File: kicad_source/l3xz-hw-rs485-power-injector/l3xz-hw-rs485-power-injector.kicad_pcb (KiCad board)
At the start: 2 copper layers, 38 x 55 mm, 14 parts, among them J1 PowerPole, J2 Conn_01x02, J3 Conn_01x03, J4 SM04B-GHS-TB, J5 EH_S4B-EH, J6 EH_S4B-EH

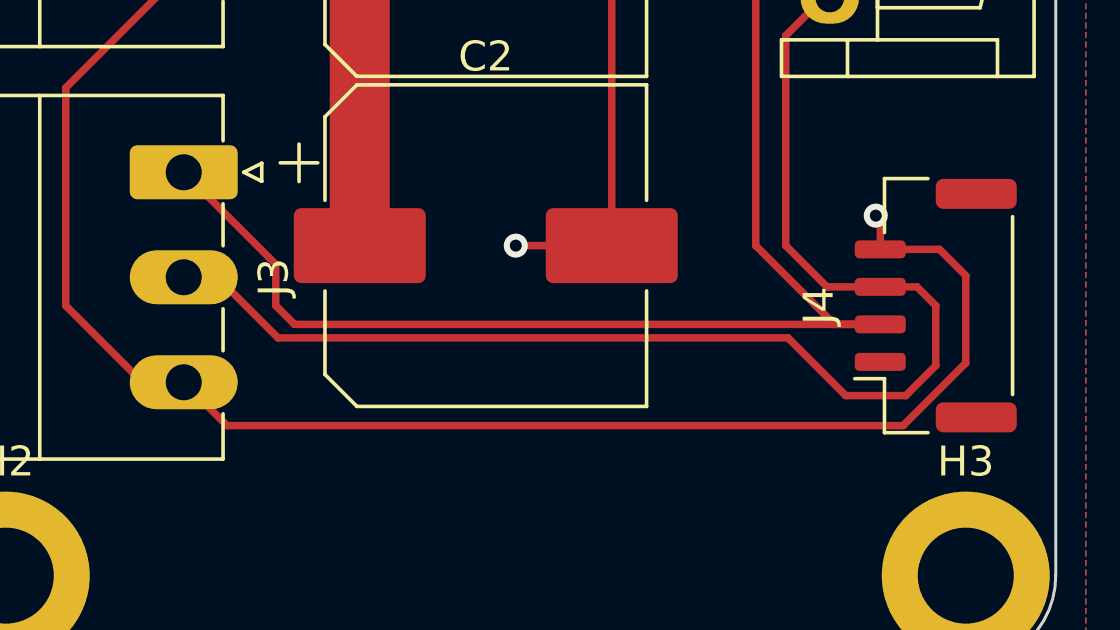
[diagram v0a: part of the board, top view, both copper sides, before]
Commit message: added resistor to connect JST GH connector to +BATT
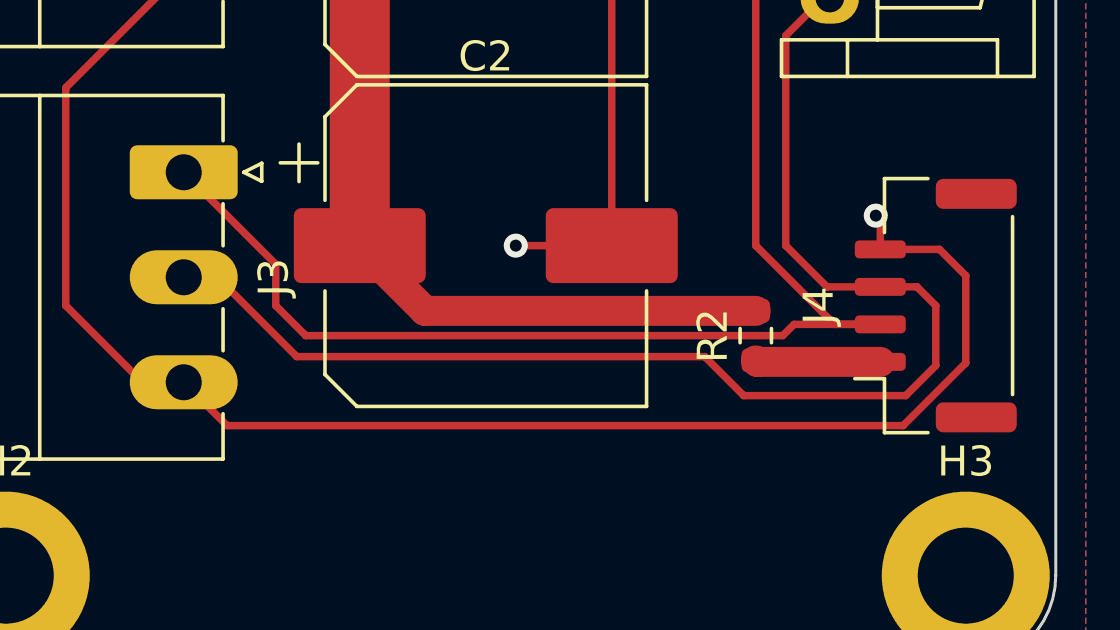
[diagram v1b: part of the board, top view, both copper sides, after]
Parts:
- added R2: DNI, Resistor_SMD:R_0603_1608Metric, F.Cu at (154.0, 97.0)
- C1, C2: value C_Polarized -> 220 uF / 50 V
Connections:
- J4 pad 1: unconnected-(J4-Pad1) -> /BATT_R
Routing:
- net +BATT: track 72.1 -> 86.2 mm
- net /BATT_R: track 0.00 -> 4.17 mm
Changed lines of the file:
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@@
   )
   (paper "A4")
+  (title_block
+    (title "l3xz-hw-rs485-power-injector")
+    (date "2023-01-21")
+    (rev "0.1")
+    (company "107-systems")
+  )
   (layers
     (0 "F.Cu" signal)
@@
   (net 3 "/RS485_A")
   (net 4 "/RS485_B")
-  (net 5 "unconnected-(J4-Pad1)")
+  (net 5 "/BATT_R")
   (net 6 "Net-(D1-Pad2)")
   (net 7 "unconnected-(H1-Pad1)")
@@
     (fp_line (start -4.125 2.45) (end 4.125 2.45) (layer "F.Fab") (width 0.1))
     (pad "1" smd roundrect (at -1.875 -1.85 90) (size 0.6 1.7) (layers "F.Cu" "F.Paste" "F.Mask") (roundrect_rratio 0.25)
-      (net 5 "unconnected-(J4-Pad1)") (pinfunction "Pin_1") (pintype "passive+no_connect"))
+      (net 5 "/BATT_R") (pinfunction "Pin_1") (pintype "passive"))
     (pad "2" smd roundrect (at -0.625 -1.85 90) (size 0.6 1.7) (layers "F.Cu" "F.Paste" "F.Mask") (roundrect_rratio 0.25)
       (net 3 "/RS485_A") (pinfunction "Pin_2") (pintype "passive"))
@@
       (effects (font (size 1 1) (thickness 0.15)))
     )
-    (fp_text value "C_Polarized" (at 0 6.3) (layer "F.Fab")
+    (fp_text value "220 uF / 50 V" (at 0 6.3) (layer "F.Fab")
       (effects (font (size 1 1) (thickness 0.15)))
     )
@@
     (model "${KICAD6_3DMODEL_DIR}/generationmake/PP 15-45 (Std)-02-08-STEP.stp"
       (offset (xyz -3.95 -13.1 16))
+      (scale (xyz 1 1 1))
+      (rotate (xyz 0 0 0))
+    )
+  )
+  (footprint "Resistor_SMD:R_0603_1608Metric" (layer "F.Cu")
+    (at 154 97 90)
+    (descr "Resistor SMD 0603 (1608 Metric), square (rectangular) end terminal, IPC_7351 nominal, (Body size source: IPC-SM-782 page 72, https://www.pcb-3d.com/wordpress/wp-content/uploads/ipc-sm-782a_amendment_1_and_2.pdf), generated with kicad-footprint-generator")
+    (tags "resistor")
+    (property "Sheetfile" "l3xz-hw-rs485-power-injector.kicad_sch")
+    (property "Sheetname" "")
+    (attr smd)
+    (fp_text reference "R2" (at 0 -1.43 90) (layer "F.SilkS")
+      (effects (font (size 1 1) (thickness 0.15)))
+    )
+    (fp_text value "DNI" (at 0 1.43 90) (layer "F.Fab")
+      (effects (font (size 1 1) (thickness 0.15)))
+    )
+    (fp_text user "${REFERENCE}" (at 0 0 90) (layer "F.Fab")
+      (effects (font (size 0.4 0.4) (thickness 0.06)))
+    )
+    (fp_line (start -0.237258 -0.5225) (end 0.237258 -0.5225) (layer "F.SilkS") (width 0.12))
+    (fp_line (start -0.237258 0.5225) (end 0.237258 0.5225) (layer "F.SilkS") (width 0.12))
+    (fp_line (start -1.48 0.73) (end -1.48 -0.73) (layer "F.CrtYd") (width 0.05))
+    (fp_line (start 1.48 -0.73) (end 1.48 0.73) (layer "F.CrtYd") (width 0.05))
+    (fp_line (start 1.48 0.73) (end -1.48 0.73) (layer "F.CrtYd") (width 0.05))
+    (fp_line (start -1.48 -0.73) (end 1.48 -0.73) (layer "F.CrtYd") (width 0.05))
+    (fp_line (start 0.8 0.4125) (end -0.8 0.4125) (layer "F.Fab") (width 0.1))
+    (fp_line (start -0.8 0.4125) (end -0.8 -0.4125) (layer "F.Fab") (width 0.1))
+    (fp_line (start 0.8 -0.4125) (end 0.8 0.4125) (layer "F.Fab") (width 0.1))
+    (fp_line (start -0.8 -0.4125) (end 0.8 -0.4125) (layer "F.Fab") (width 0.1))
+    (pad "1" smd roundrect (at -0.825 0 90) (size 0.8 0.95) (layers "F.Cu" "F.Paste" "F.Mask") (roundrect_rratio 0.25)
+      (net 5 "/BATT_R") (pintype "passive"))
+    (pad "2" smd roundrect (at 0.825 0 90) (size 0.8 0.95) (layers "F.Cu" "F.Paste" "F.Mask") (roundrect_rratio 0.25)
+      (net 1 "+BATT") (pintype "passive"))
+    (model "${KICAD6_3DMODEL_DIR}/Resistor_SMD.3dshapes/R_0603_1608Metric.wrl"
+      (offset (xyz 0 0 0))
       (scale (xyz 1 1 1))
       (rotate (xyz 0 0 0))
@@
       (effects (font (size 1 1) (thickness 0.15)))
     )
-    (fp_text value "C_Polarized" (at 0 6.3) (layer "F.Fab")
+    (fp_text value "220 uF / 50 V" (at 0 6.3) (layer "F.Fab")
       (effects (font (size 1 1) (thickness 0.15)))
     )
@@
   (segment (start 149 66.175) (end 147.73 64.905) (width 0.25) (layer "F.Cu") (net 1))
   (segment (start 150.905 64.905) (end 144.1825 64.905) (width 1) (layer "F.Cu") (net 1))
+  (segment (start 154 96.175) (end 142.975 96.175) (width 1) (layer "F.Cu") (net 1))
   (segment (start 140.8 68.2875) (end 144.1825 64.905) (width 2) (layer "F.Cu") (net 1))
   (segment (start 152.75 66.75) (end 150.905 64.905) (width 1) (layer "F.Cu") (net 1))
   (segment (start 156.4675 80.75) (end 143.05 80.75) (width 1) (layer "F.Cu") (net 1))
+  (segment (start 142.975 96.175) (end 140.8 94) (width 1) (layer "F.Cu") (net 1))
   (segment (start 140.8 94) (end 140.8 83) (width 2) (layer "F.Cu") (net 1))
   (segment (start 139.105 81.305) (end 140.8 83) (width 2) (layer "F.Cu") (net 1))
@@
   (via (at 158 93) (size 0.8) (drill 0.4) (layers "F.Cu" "B.Cu") (net 2))
   (via (at 146 83) (size 0.8) (drill 0.4) (layers "F.Cu" "B.Cu") (net 2))
-  (segment (start 158.15 96.625) (end 138.625 96.625) (width 0.25) (layer "F.Cu") (net 3))
+  (segment (start 158.15 96.625) (end 155.275 96.625) (width 0.25) (layer "F.Cu") (net 3))
   (segment (start 156.4675 83.25) (end 157.75 83.25) (width 0.25) (layer "F.Cu") (net 3))
   (segment (start 154 94) (end 154 85) (width 0.25) (layer "F.Cu") (net 3))
   (segment (start 155 72.069201) (end 155 70) (width 0.25) (layer "F.Cu") (net 3))
-  (segment (start 138.625 96.625) (end 138 96) (width 0.25) (layer "F.Cu") (net 3))
-  (segment (start 138 96) (end 138 94.6225) (width 0.25) (layer "F.Cu") (net 3))
   (segment (start 155.75 69.25) (end 156.4675 69.25) (width 0.25) (layer "F.Cu") (net 3))
   (segment (start 155 70) (end 155.75 69.25) (width 0.25) (layer "F.Cu") (net 3))
   (segment (start 157.930799 75) (end 155 72.069201) (width 0.25) (layer "F.Cu") (net 3))
+  (segment (start 154.9 97) (end 139 97) (width 0.25) (layer "F.Cu") (net 3))
+  (segment (start 139 97) (end 138 96) (width 0.25) (layer "F.Cu") (net 3))
   (segment (start 155.75 83.25) (end 154 85) (width 0.25) (layer "F.Cu") (net 3))
   (segment (start 157.75 83.25) (end 159 82) (width 0.25) (layer "F.Cu") (net 3))
   (segment (start 156.4675 83.25) (end 155.75 83.25) (width 0.25) (layer "F.Cu") (net 3))
+  (segment (start 138 94.6225) (end 134.9325 91.555) (width 0.25) (layer "F.Cu") (net 3))
   (segment (start 159 76) (end 158 75) (width 0.25) (layer "F.Cu") (net 3))
+  (segment (start 138 96) (end 138 94.6225) (width 0.25) (layer "F.Cu") (net 3))
   (segment (start 158 75) (end 157.930799 75) (width 0.25) (layer "F.Cu") (net 3))
-  (segment (start 138 94.6225) (end 134.9325 91.555) (width 0.25) (layer "F.Cu") (net 3))
+  (segment (start 155.275 96.625) (end 154.9 97) (width 0.25) (layer "F.Cu") (net 3))
   (segment (start 156.625 96.625) (end 154 94) (width 0.25) (layer "F.Cu") (net 3))
   (segment (start 158.15 96.625) (end 156.625 96.625) (width 0.25) (layer "F.Cu") (net 3))
   (segment (start 159 82) (end 159 76) (width 0.25) (layer "F.Cu") (net 3))
-  (segment (start 138.075 97.075) (end 155.075 97.075) (width 0.25) (layer "F.Cu") (net 4))
-  (segment (start 136.055 95.055) (end 138.075 97.075) (width 0.25) (layer "F.Cu") (net 4))
+  (segment (start 160 96) (end 160 98) (width 0.25) (layer "F.Cu") (net 4))
+  (segment (start 159.375 95.375) (end 160 96) (width 0.25) (layer "F.Cu") (net 4))
   (segment (start 156.25 85.75) (end 156.4675 85.75) (width 0.25) (layer "F.Cu") (net 4))
   (segment (start 156.4675 85.75) (end 157.25 85.75) (width 0.25) (layer "F.Cu") (net 4))
   (segment (start 158.15 95.375) (end 156.375 95.375) (width 0.25) (layer "F.Cu") (net 4))
-  (segment (start 159.375 95.375) (end 158.15 95.375) (width 0.25) (layer "F.Cu") (net 4))
   (segment (start 156.75 71.75) (end 156.4675 71.75) (width 0.25) (layer "F.Cu") (net 4))
   (segment (start 155 87) (end 156.25 85.75) (width 0.25) (layer "F.Cu") (net 4))
-  (segment (start 155.075 97.075) (end 157 99) (width 0.25) (layer "F.Cu") (net 4))
   (segment (start 156.375 95.375) (end 155 94) (width 0.25) (layer "F.Cu") (net 4))
-  (segment (start 160 98) (end 160 96) (width 0.25) (layer "F.Cu") (net 4))
-  (segment (start 134.9325 95.055) (end 136.055 95.055) (width 0.25) (layer "F.Cu") (net 4))
+  (segment (start 136.055 95.055) (end 134.9325 95.055) (width 0.25) (layer "F.Cu") (net 4))
+  (segment (start 158.15 95.375) (end 159.375 95.375) (width 0.25) (layer "F.Cu") (net 4))
+  (segment (start 153.6 99) (end 152.3 97.7) (width 0.25) (layer "F.Cu") (net 4))
   (segment (start 160 83) (end 160 75) (width 0.25) (layer "F.Cu") (net 4))
-  (segment (start 160 96) (end 159.375 95.375) (width 0.25) (layer "F.Cu") (net 4))
-  (segment (start 159 99) (end 160 98) (width 0.25) (layer "F.Cu") (net 4))
   (segment (start 155 94) (end 155 87) (width 0.25) (layer "F.Cu") (net 4))
-  (segment (start 157 99) (end 159 99) (width 0.25) (layer "F.Cu") (net 4))
+  (segment (start 152.3 97.7) (end 138.7 97.7) (width 0.25) (layer "F.Cu") (net 4))
+  (segment (start 160 98) (end 159 99) (width 0.25) (layer "F.Cu") (net 4))
+  (segment (start 138.7 97.7) (end 136.055 95.055) (width 0.25) (layer "F.Cu") (net 4))
   (segment (start 160 75) (end 156.75 71.75) (width 0.25) (layer "F.Cu") (net 4))
+  (segment (start 159 99) (end 153.6 99) (width 0.25) (layer "F.Cu") (net 4))
   (segment (start 157.25 85.75) (end 160 83) (width 0.25) (layer "F.Cu") (net 4))
+  (segment (start 158.15 97.875) (end 154.05 97.875) (width 1) (layer "F.Cu") (net 5))
+  (segment (start 154.05 97.875) (end 154 97.825) (width 1) (layer "F.Cu") (net 5))
   (segment (start 149 70.2125) (end 149 67.825) (width 0.25) (layer "F.Cu") (net 6))
   (zone (net 2) (net_name "GND") (layer "F.Cu") (hatch edge 0.508)

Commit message: added RS-485 transceiver and status LED
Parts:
- added C3: 100 nF, Capacitor_SMD:C_0603_1608Metric, F.Cu at (147.1, 64.0)
- added C4: 100 nF, Capacitor_SMD:C_0603_1608Metric, F.Cu at (156.4, 55.8)
- added C5: 1 uF, Capacitor_SMD:C_0603_1608Metric, F.Cu at (146.3, 61.6)
- added D2: LED green, LED_SMD:LED_0603_1608Metric, F.Cu at (145.3, 54.4)
- added J7: Conn_01x04, Connector_PinHeader_2.54mm:PinHeader_1x04_P2.54mm_Vertical, F.Cu at (141.6, 54.7)
- added R3: 10k, Resistor_SMD:R_0603_1608Metric, F.Cu at (145.3, 56.0)
- added R4: 10k, Resistor_SMD:R_0603_1608Metric, F.Cu at (145.3, 57.6)
- added U1: L78L05_SOT89, Package_TO_SOT_SMD:SOT-89-3, F.Cu at (150.5, 63.2)
- added U2: SN75176AD, Package_SO:SOIC-8_3.9x4.9mm_P1.27mm, F.Cu at (151.5, 57.0)
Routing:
- net /RS485_RX: track 0.00 -> 24.4 mm
- net /RS485_B: track 61.5 -> 81.7 mm
- net /RS485_A: track 62.4 -> 78.3 mm
- net +5V: track 0.00 -> 14.8 mm
- net /RS485_TX: track 0.00 -> 12.2 mm
- net /RS485_TXEN: track 0.00 -> 11.7 mm
- net GND: track 75.3 -> 79.2 mm, vias 3 -> 6
- net Net-(D2-Pad2): track 0.00 -> 1.62 mm
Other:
- board text added: "bot"
- board text added: "top"

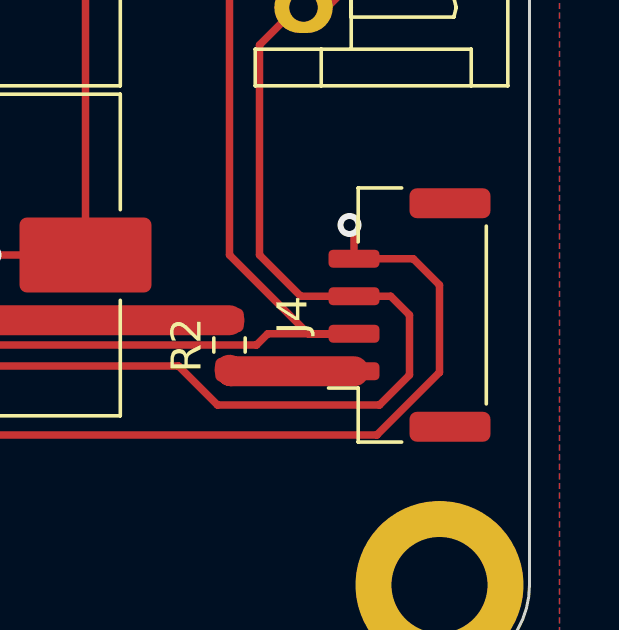
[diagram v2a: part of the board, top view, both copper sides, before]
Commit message: added mounting pad on JST GH connector
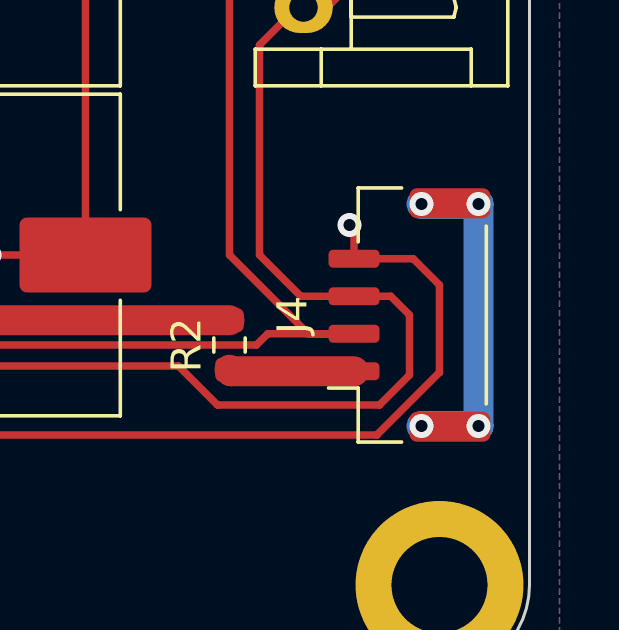
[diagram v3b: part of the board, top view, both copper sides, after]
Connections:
- J4 pad MP: (no net) -> /MP
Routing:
- net /MP: track 0.00 -> 11.2 mm, vias 0 -> 4
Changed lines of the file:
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@@
   (net 14 "/RS485_TX")
   (net 15 "/RS485_RX")
+  (net 16 "/MP")
   (footprint "Resistor_SMD:R_0603_1608Metric" (layer "F.Cu")
     (at 149 67 -90)
@@
     (pad "4" smd roundrect (at 1.875 -1.85 90) (size 0.6 1.7) (layers "F.Cu" "F.Paste" "F.Mask") (roundrect_rratio 0.25)
       (net 2 "GND") (pinfunction "Pin_4") (pintype "passive"))
-    (pad "MP" smd roundrect (at -3.725 1.35 90) (size 1 2.7) (layers "F.Cu" "F.Paste" "F.Mask") (roundrect_rratio 0.25))
-    (pad "MP" smd roundrect (at 3.725 1.35 90) (size 1 2.7) (layers "F.Cu" "F.Paste" "F.Mask") (roundrect_rratio 0.25))
+    (pad "MP" smd roundrect (at -3.725 1.35 90) (size 1 2.7) (layers "F.Cu" "F.Paste" "F.Mask") (roundrect_rratio 0.25)
+      (net 16 "/MP") (pinfunction "MountPin") (pintype "passive"))
+    (pad "MP" smd roundrect (at 3.725 1.35 90) (size 1 2.7) (layers "F.Cu" "F.Paste" "F.Mask") (roundrect_rratio 0.25)
+      (net 16 "/MP") (pinfunction "MountPin") (pintype "passive"))
     (model "${KICAD6_3DMODEL_DIR}/Connector_JST.3dshapes/JST_GH_SM04B-GHS-TB_1x04-1MP_P1.25mm_Horizontal.wrl"
       (offset (xyz 0 0 0))
@@
   (segment (start 146.125 56) (end 147.03 55.095) (width 0.25) (layer "F.Cu") (net 15))
   (segment (start 149.025 55.095) (end 149.795 55.095) (width 0.25) (layer "F.Cu") (net 15))
+  (via (at 162.3 99.7) (size 0.8) (drill 0.4) (layers "F.Cu" "B.Cu") (net 16))
+  (via (at 160.4 92.3) (size 0.8) (drill 0.4) (layers "F.Cu" "B.Cu") (net 16))
+  (via (at 160.4 99.7) (size 0.8) (drill 0.4) (layers "F.Cu" "B.Cu") (net 16))
+  (via (at 162.3 92.3) (size 0.8) (drill 0.4) (layers "F.Cu" "B.Cu") (net 16))
+  (segment (start 162.3 92.3) (end 162.3 99.7) (width 1) (layer "B.Cu") (net 16))
+  (segment (start 160.4 99.7) (end 162.3 99.7) (width 1) (layer "B.Cu") (net 16))
+  (segment (start 160.4 92.3) (end 162.3 92.3) (width 1) (layer "B.Cu") (net 16))
   (zone (net 2) (net_name "GND") (layer "F.Cu") (hatch edge 0.508)
     (connect_pads (clearance 0.508))

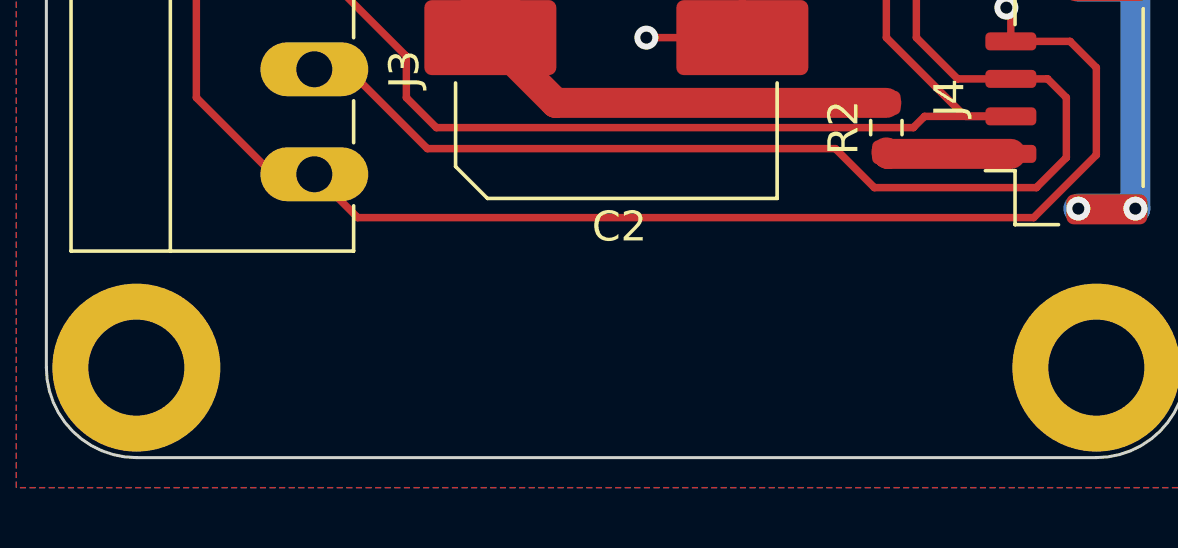
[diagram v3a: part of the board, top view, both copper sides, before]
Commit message: added some labels
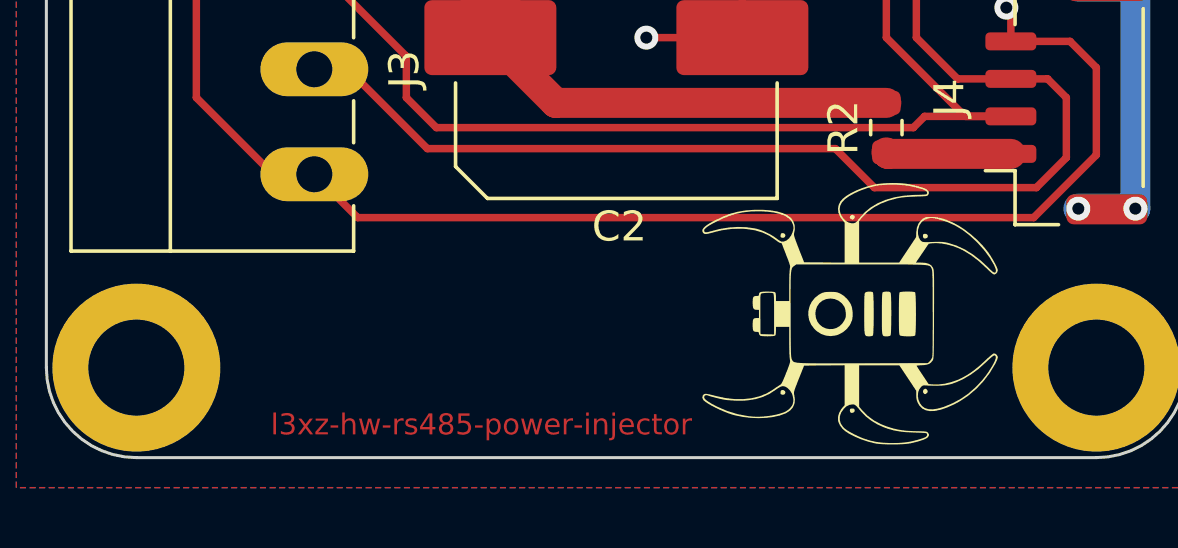
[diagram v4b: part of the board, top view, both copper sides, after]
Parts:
- added L1: Label, generationmake:generationmake_small_solder, F.Cu at (139.7, 107.0)
- added L2: Label, generationmake:l3xz_silk, B.Cu at (146.8, 82.7)
- added L3: Label, generationmake:l3xz_small_silk, F.Cu at (152.8, 103.2)
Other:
- board text added: "l3xz-hw-rs485-power-injector"
